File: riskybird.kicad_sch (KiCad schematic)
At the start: 85 parts, among them J1 USB_B_Micro, J2 Conn_01x02, J3 Conn_01x02, J4 Conn_01x02, J5 Conn_01x02, J6 Conn_01x02, Q1 Q_NMOS_GSD, Q2 Q_NMOS_GSD, Q3 Q_NMOS_GSD, Q4 Q_NMOS_GSD, Q5 DNBT8105-7, Q6 DNBT8105-7, Q7 Q_NMOS_GSD, SW1 SW_SPST, SW2 SW_SPST, SW3 SW_SPST, U1 MCP73831-2-OT, U2 MPU-9150, U3 TPS2113A, U4 LP2985-3.0, U5 MPL3115A2, U6 ESP32-C3-WROOM-02, U8 FT231XS

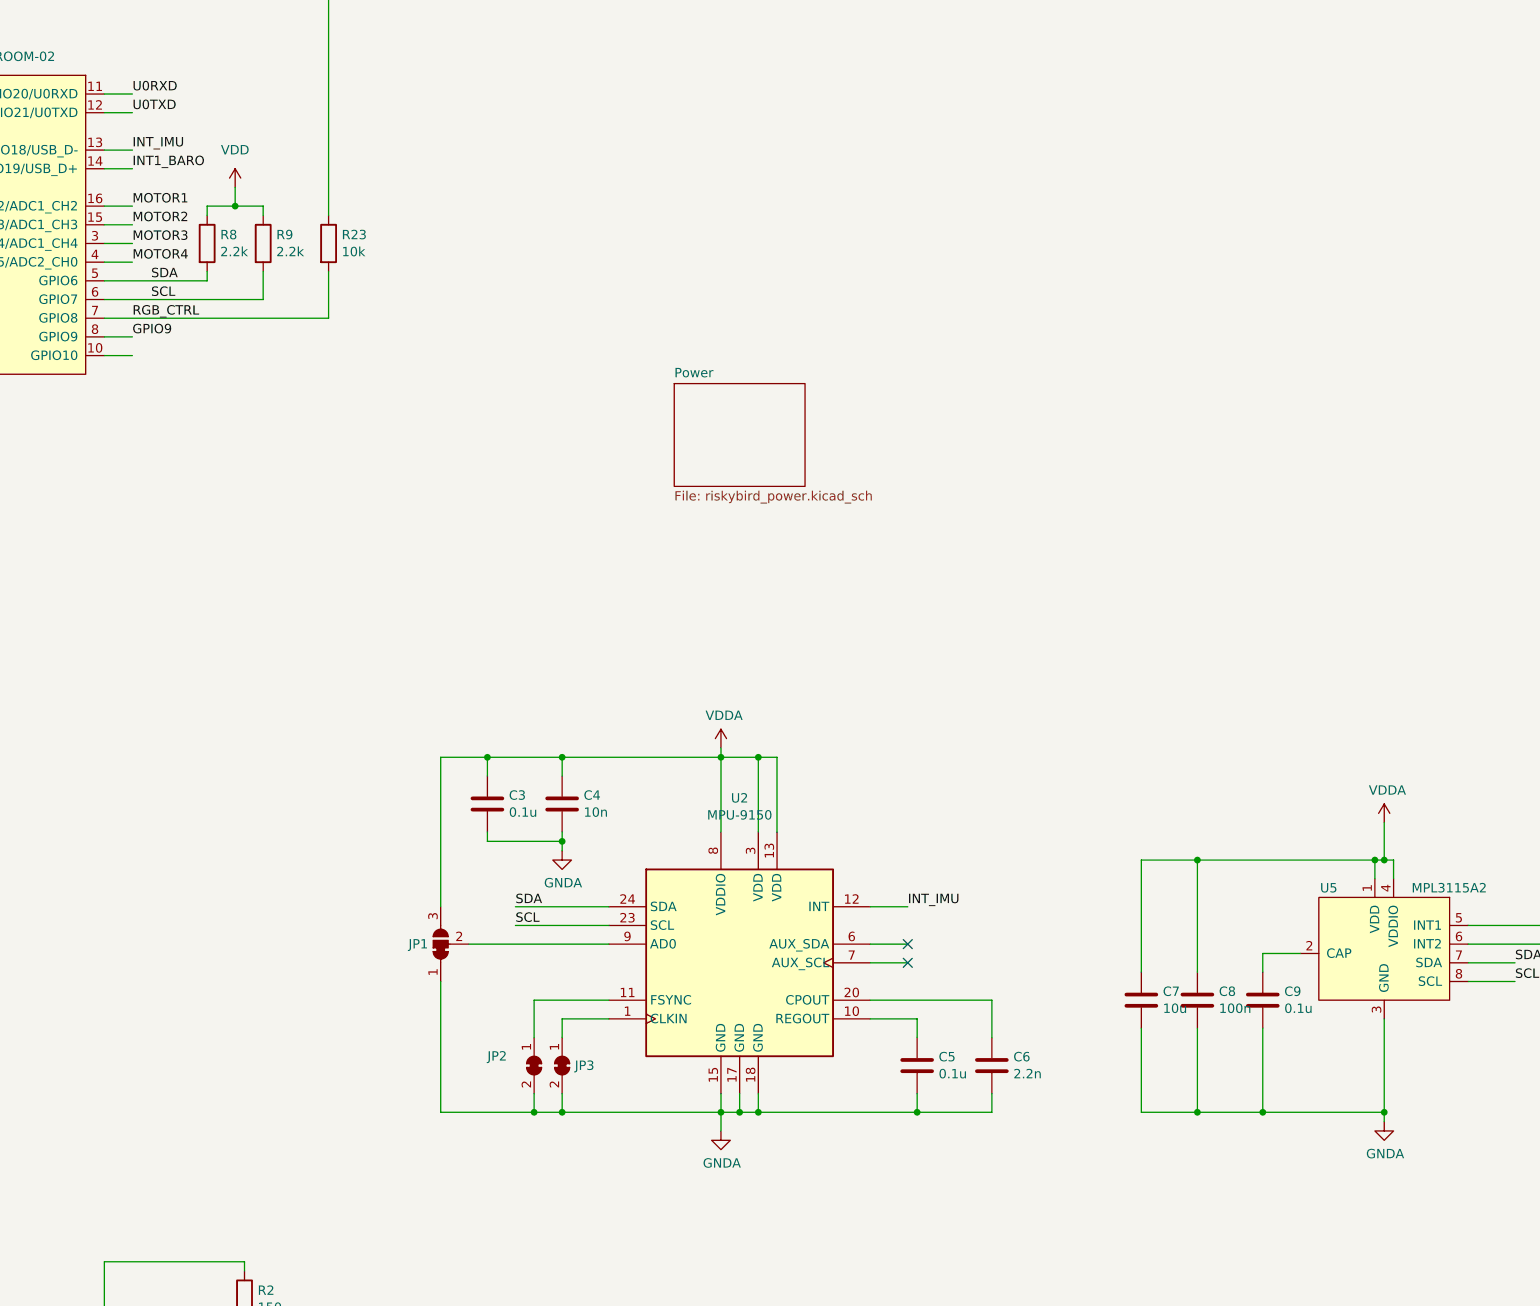
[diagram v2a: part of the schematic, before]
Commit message: add new BMI088 IMU
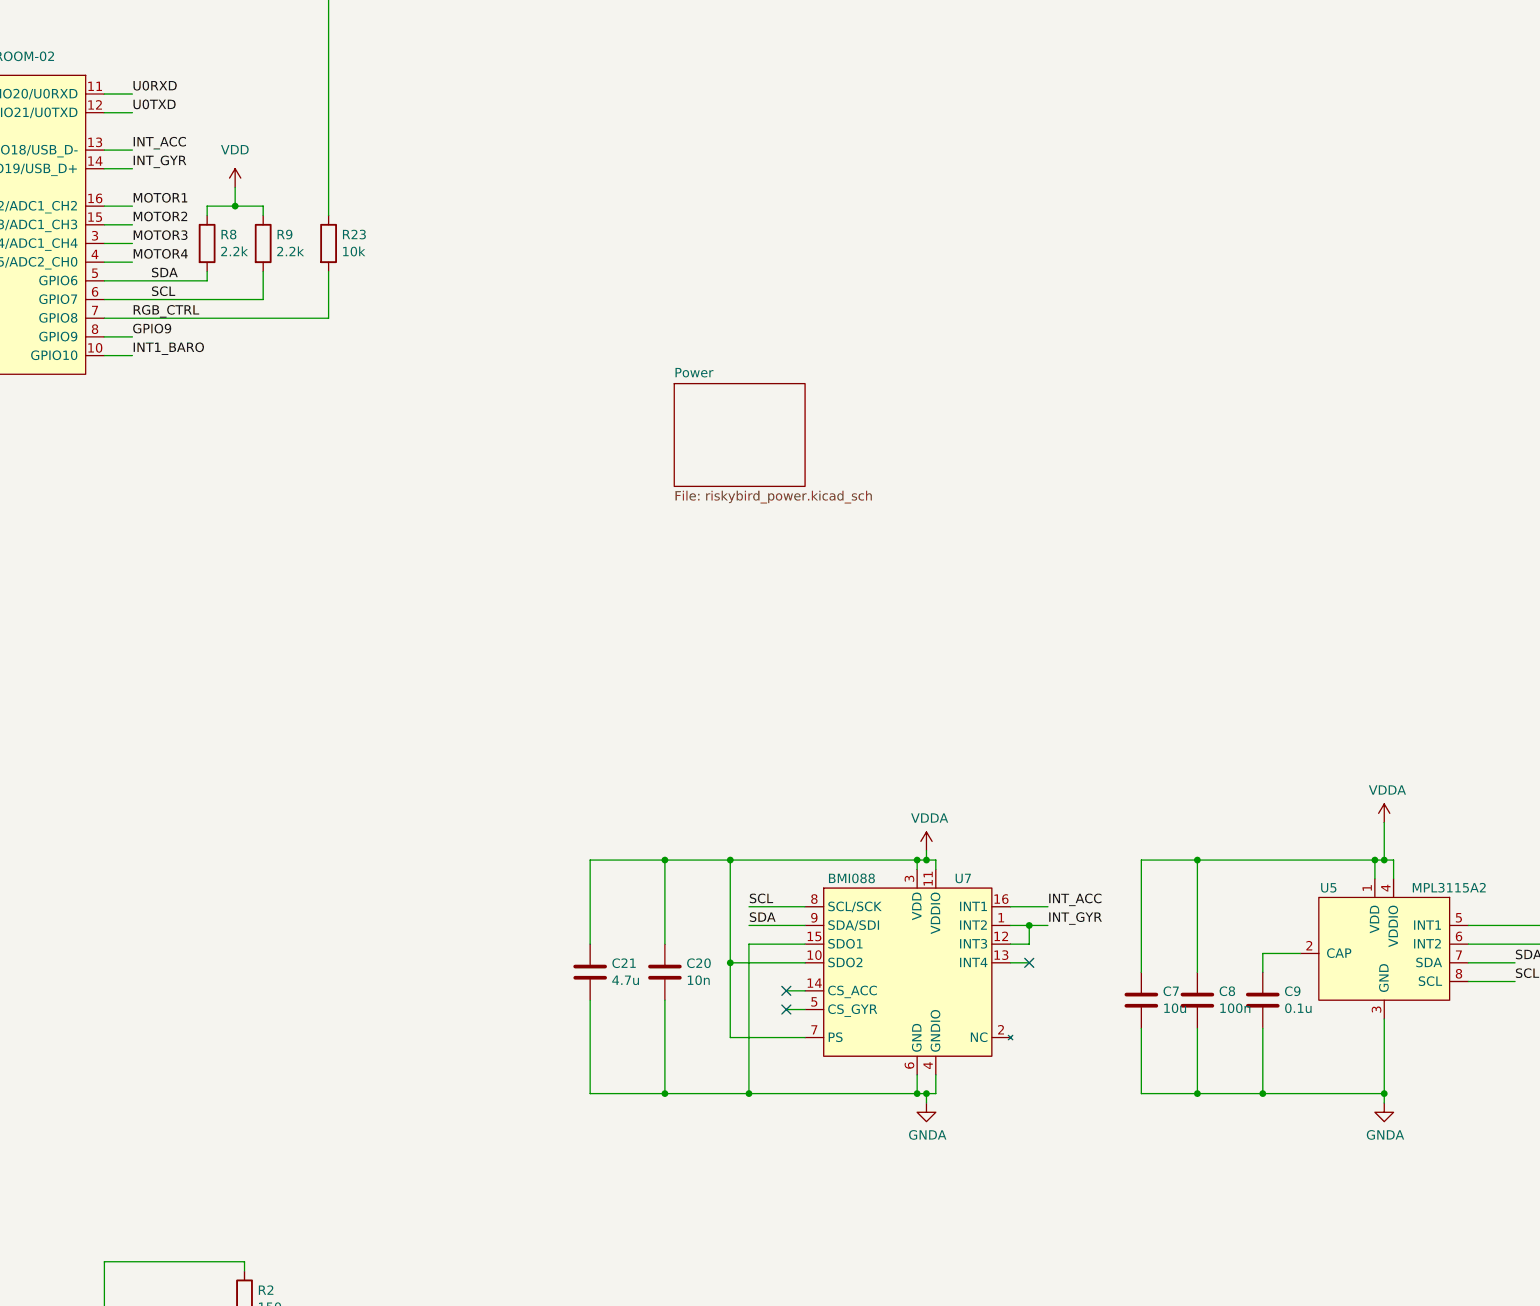
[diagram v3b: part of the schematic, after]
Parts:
- removed C3, C5: 0.1u, Capacitor_SMD:C_0603_1608Metric_Pad1.08x0.95mm_HandSolder, symbol Device:C
- removed C4: 10n, Capacitor_SMD:C_0603_1608Metric_Pad1.08x0.95mm_HandSolder, symbol Device:C
- removed C6: 2.2n, Capacitor_SMD:C_0603_1608Metric_Pad1.08x0.95mm_HandSolder, symbol Device:C
- removed JP1: SolderJumper_3_Bridged12, Jumper:SolderJumper-3_P1.3mm_Bridged12_Pad1.0x1.5mm, symbol riskybird-rescue:SolderJumper_3_Bridged12-Jumper
- removed JP2, JP3: SolderJumper_2_Bridged, Jumper:SolderJumper-2_P1.3mm_Bridged_Pad1.0x1.5mm, symbol Jumper:SolderJumper_2_Bridged
- removed U2: MPU-9150, Sensor_Motion:InvenSense_QFN-24_4x4mm_P0.5mm, symbol riskybird-rescue:MPU-9150-Sensor_Motion
- added C20: 10n, Capacitor_SMD:C_0603_1608Metric_Pad1.08x0.95mm_HandSolder, symbol Device:C
- added C21: 4.7u, Capacitor_SMD:C_0603_1608Metric_Pad1.08x0.95mm_HandSolder, symbol Device:C
- added U7: BMI088, riskybird:BMI088_Handsolder, symbol riskybird:BMI088
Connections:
- net GND: now also C20.2, C21.2, U7.15 (SDO1), U7.4 (GNDIO), U7.6 (GND)
- net INT1_BARO: now also U6.10 (GPIO10); no longer U6.14 (GPIO19/USB_D+)
- net SCL: now also U7.8 (SCL/SCK)
- net SDA: now also U7.9 (SDA/SDI)
- net VDDA: now also C20.1, C21.1, U7.10 (SDO2), U7.11 (VDDIO), U7.3 (VDD), U7.7 (PS)
- net INT_IMU renamed INT_ACC
- net INT_ACC: now also U7.16 (INT1)
- new net INT_GYR: U6.14 (GPIO19/USB_D+), U7.1 (INT2), U7.12 (INT3)
- no-connect marks 13 -> 14

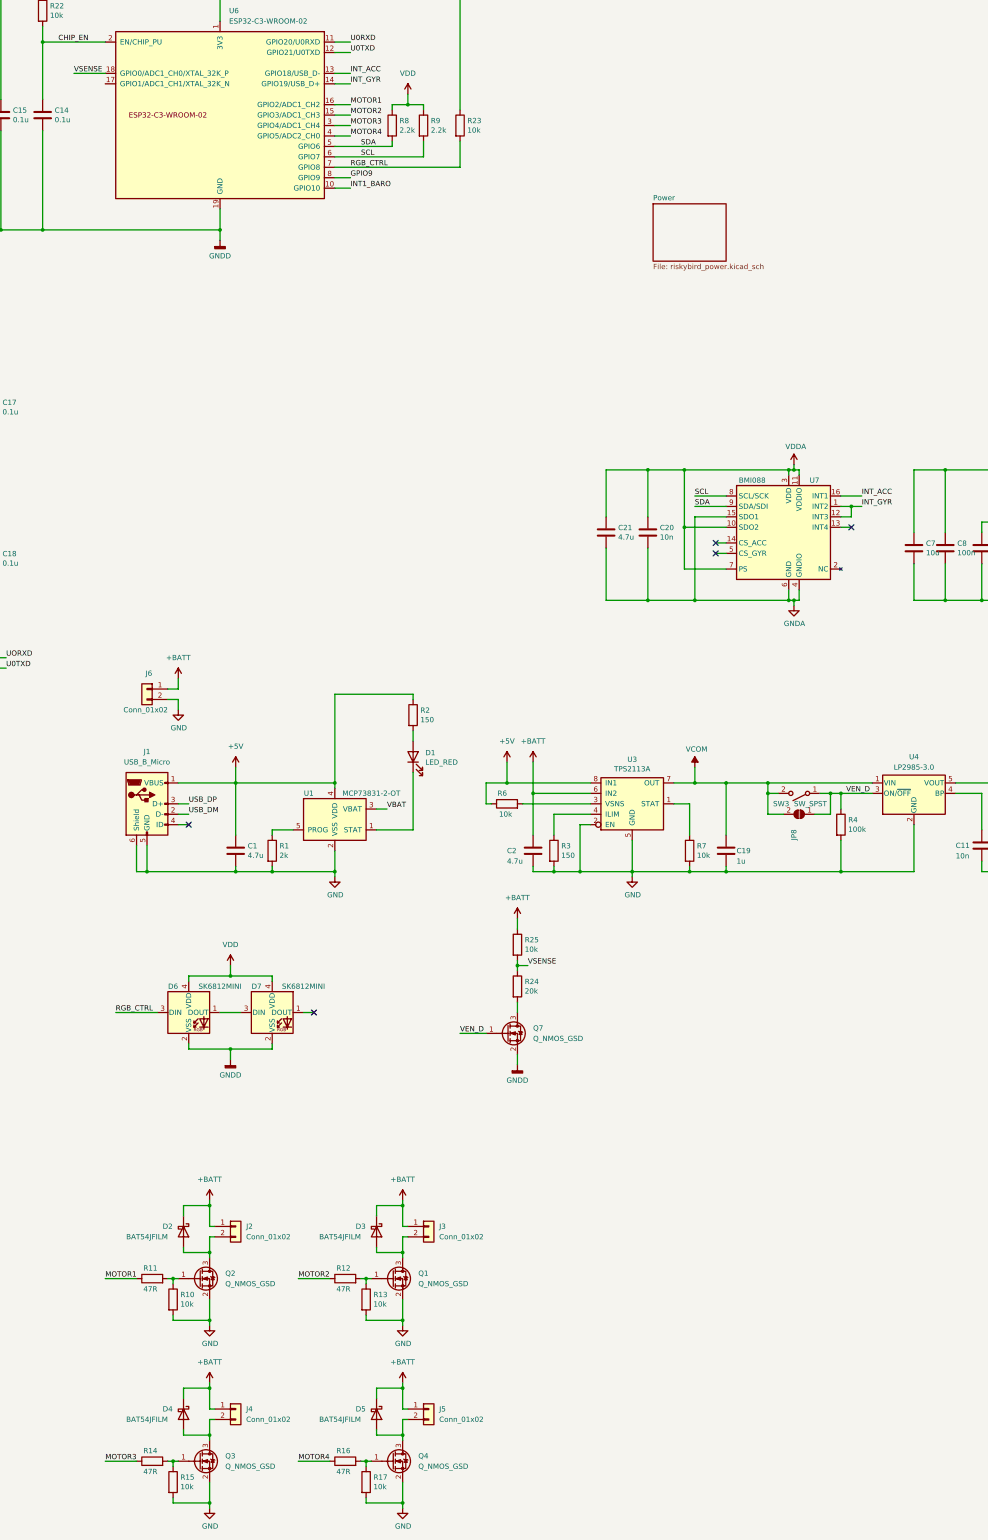
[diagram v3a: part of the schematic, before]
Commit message: update footprints, begin placement
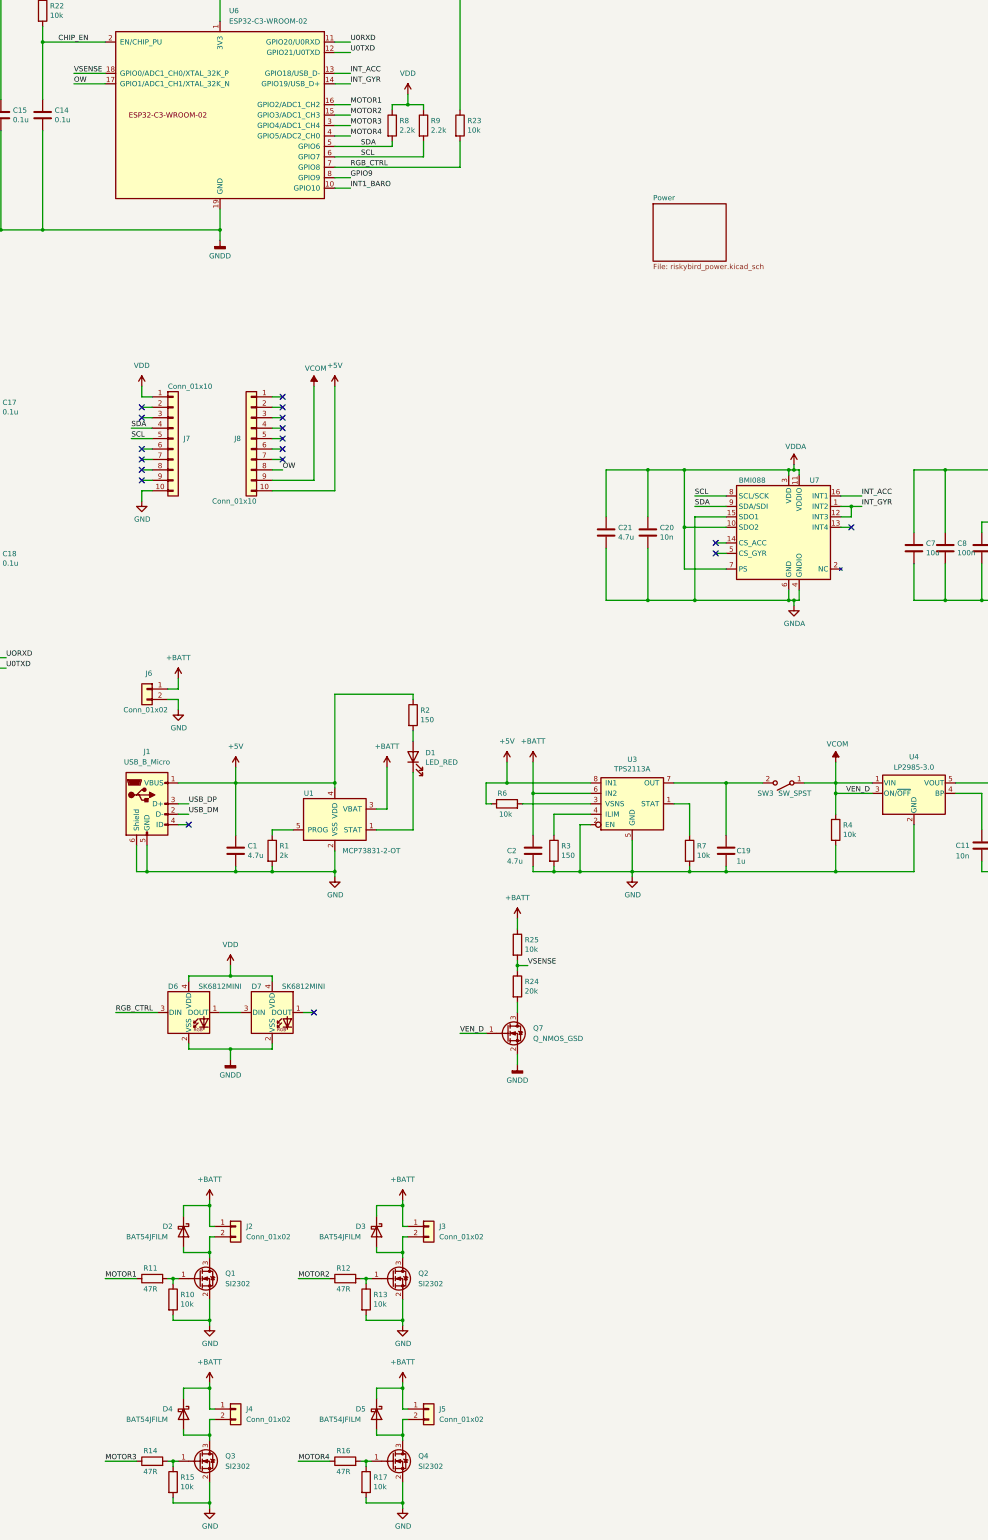
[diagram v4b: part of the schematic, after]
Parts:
- removed JP8: SolderJumper_2_Open, Jumper:SolderJumper-2_P1.3mm_Open_Pad1.0x1.5mm, symbol Jumper:SolderJumper_2_Open
- added J7, J8: Conn_01x10, riskybird:PinHeader_1x10_P2.00mm_Vertical_SMD_Pin1Right_THT, symbol Connector_Generic:Conn_01x10
- J6: footprint (none) -> Connector_PinHeader_2.54mm:PinHeader_1x02_P2.54mm_Vertical
- L1: footprint (none) -> Inductor_SMD:L_0805_2012Metric_Pad1.15x1.40mm_HandSolder
- Q1: renamed from Q2; value Q_NMOS_GSD -> SI2302; footprint (none) -> Package_TO_SOT_SMD:SOT-23
- Q2: renamed from Q1; value Q_NMOS_GSD -> SI2302; footprint (none) -> Package_TO_SOT_SMD:SOT-23
- Q3, Q4: value Q_NMOS_GSD -> SI2302; footprint (none) -> Package_TO_SOT_SMD:SOT-23
- Q5, Q6: footprint Package_TO_SOT_SMD:SOT-23_Handsoldering -> Package_TO_SOT_SMD:SOT-23
- Q7: footprint (none) -> Package_TO_SOT_SMD:SOT-23
- R23, R8, R9: footprint Resistor_SMD:R_0805_2012Metric_Pad1.20x1.40mm_HandSolder -> Resistor_SMD:R_0603_1608Metric_Pad0.98x0.95mm_HandSolder
- R4: value 100k -> 10k
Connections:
- net VBAT is gone; now on net +BATT: U1.3 (VBAT)
- net VEN_D is gone; now on net VCOM: Q7.1 (G), R4.1, SW3.1 (A), U4.3 (ON/~{OFF})
- net +5V: now also J8.10 (Pin_10)
- net GND: now also J7.10 (Pin_10)
- net SCL: now also J7.5 (Pin_5)
- net SDA: now also J7.4 (Pin_4)
- net VCOM: now also J8.9 (Pin_9); no longer C19.1, SW3.2 (B), U3.7 (OUT)
- net VDD: now also J7.1 (Pin_1)
- net OW: now reaches U6.17 (GPIO1/ADC1_CH1/XTAL_32K_N)
- net OW: now also J8.8 (Pin_8)
- new net: C19.1, SW3.2 (B), U3.7 (OUT)
- no-connect marks 14 -> 27
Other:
- moved on the sheet: SW3

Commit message: almost done routing
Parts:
- removed C7: 10u, Capacitor_SMD:C_0603_1608Metric_Pad1.08x0.95mm_HandSolder, symbol Device:C
- removed C8: 100n, Capacitor_SMD:C_0603_1608Metric_Pad1.08x0.95mm_HandSolder, symbol Device:C
- removed C9: 0.1u, Capacitor_SMD:C_0603_1608Metric_Pad1.08x0.95mm_HandSolder, symbol Device:C
- removed JP4, JP5, JP7: SolderJumper_2_Bridged, Jumper:SolderJumper-2_P1.3mm_Bridged_Pad1.0x1.5mm, symbol Jumper:SolderJumper_2_Bridged
- removed U5: MPL3115A2, riskybird:MPL3115A2, symbol riskybird-rescue:MPL3115A2-slice
- added C3, C4: 100n, Capacitor_SMD:C_0603_1608Metric_Pad1.08x0.95mm_HandSolder, symbol Device:C
- added C5, C6: 0.1u, Capacitor_SMD:C_0603_1608Metric_Pad1.08x0.95mm_HandSolder, symbol Device:C
- added JP1, JP2: SolderJumper_2_Bridged, Jumper:SolderJumper-2_P1.3mm_Bridged_Pad1.0x1.5mm, symbol Jumper:SolderJumper_2_Bridged
- added U2: ~, riskybird:BMP390_Handsolder, symbol riskybird:BMP390
- added U5, U9: ~, Package_TO_SOT_SMD:SOT-363_SC-70-6, symbol riskybird:74LVC1G157
- JP6: footprint Jumper:SolderJumper-2_P1.3mm_Bridged_Pad1.0x1.5mm -> Jumper:SolderJumper-2_P1.3mm_Open_Pad1.0x1.5mm; symbol Jumper:SolderJumper_2_Bridged -> Jumper:SolderJumper_2_Open
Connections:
- net UORXD is gone; now on net U0RXD: JP6.2 (B)
- net +5V: now also U5.6 (S), U9.6 (S)
- net +BATT: now also J2.2 (Pin_2), J4.2 (Pin_2); no longer J2.1 (Pin_1), J4.1 (Pin_1)
- net GND: now also JP1.1 (A); no longer C10.2, C11.2, C12.2, C13.2, C14.2, C15.2, C16.2, C17.2, C18.2, C20.2, C21.2, D6.2 (VSS), D7.2 (VSS), D8.1 (K), Q7.2 (S), R4.2, SW1.1 (A), SW2.1 (A), U6.19 (GND), U6.9 (GND), U7.15 (SDO1), U7.4 (GNDIO), U7.6 (GND), U8.16 (GND), U8.6 (GND)
- net SCL: now also U2.2 (SCL/SCK)
- net SDA: now also U2.4 (SDA/SDI)
- net U0RXD: now also U5.4
- net U0TXD: now also U8.4 (RXD), U9.3 (I0)
- net VDD: now also C5.1, C6.1, U5.5 (VCC), U9.1 (I1), U9.5 (VCC)
- net VDDA: now also C3.1, C4.1, U2.1 (VDDIO), U2.10 (VDD), U2.6 (CSB)
- net at D4.2 (A), Q3.3 (D): now also J4.1 (Pin_1); no longer J4.2 (Pin_2)
- net at D2.2 (A), Q1.3 (D): now also J2.1 (Pin_1); no longer J2.2 (Pin_2)
- net FTRXD: now reaches JP6.1 (A), U8.20 (TXD)
- net FTRXD: now also U5.1 (I1)
- net SRXD: now reaches J7.2 (Pin_2)
- net SRXD: now also U5.3 (I0)
- net STXD: now reaches J7.3 (Pin_3)
- net STXD: now also U9.4
- net INT1_BARO renamed INT_BARO
- net INT_BARO: now also U2.7 (INT)
- new net GNDA: C12.2, C20.2, C21.2, C3.2, C4.2, JP2.2 (B), U2.3 (VSS), U2.5 (ADR/SDO), U2.8 (VSS), U2.9 (VSS), U7.15 (SDO1), U7.4 (GNDIO), U7.6 (GND)
- new net GNDD: C10.2, C11.2, C13.2, C14.2, C15.2, C16.2, C17.2, C18.2, C5.2, C6.2, D6.2 (VSS), D7.2 (VSS), D8.1 (K), JP1.2 (B), JP2.1 (A), Q7.2 (S), R4.2, SW1.1 (A), SW2.1 (A), U5.2 (GND), U6.19 (GND), U6.9 (GND), U8.16 (GND), U8.6 (GND), U9.2 (GND)
- no-connect marks 27 -> 25
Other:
- note added: "ADDR = 111011X"
- note added: "TODO Check Motor Polarity"

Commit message: minor changes
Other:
- note removed: "TODO Check Motor Polarity"
- moved on the sheet: C20, C21, C5, C6, J6, U5, U7, U9
